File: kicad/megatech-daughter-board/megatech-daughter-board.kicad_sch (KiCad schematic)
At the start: 41 parts, among them CN1 JST NH 7P, CN2 DB25_Socket, CN3 Conn_02x20_Counter_Clockwise, IC1 Z084000xP, IC2 NEC D71051C, IC3 HC393, IC4 HC04, IC5 PAL16L8A, IC6 µPD4711C, X1 4.9152 MHz

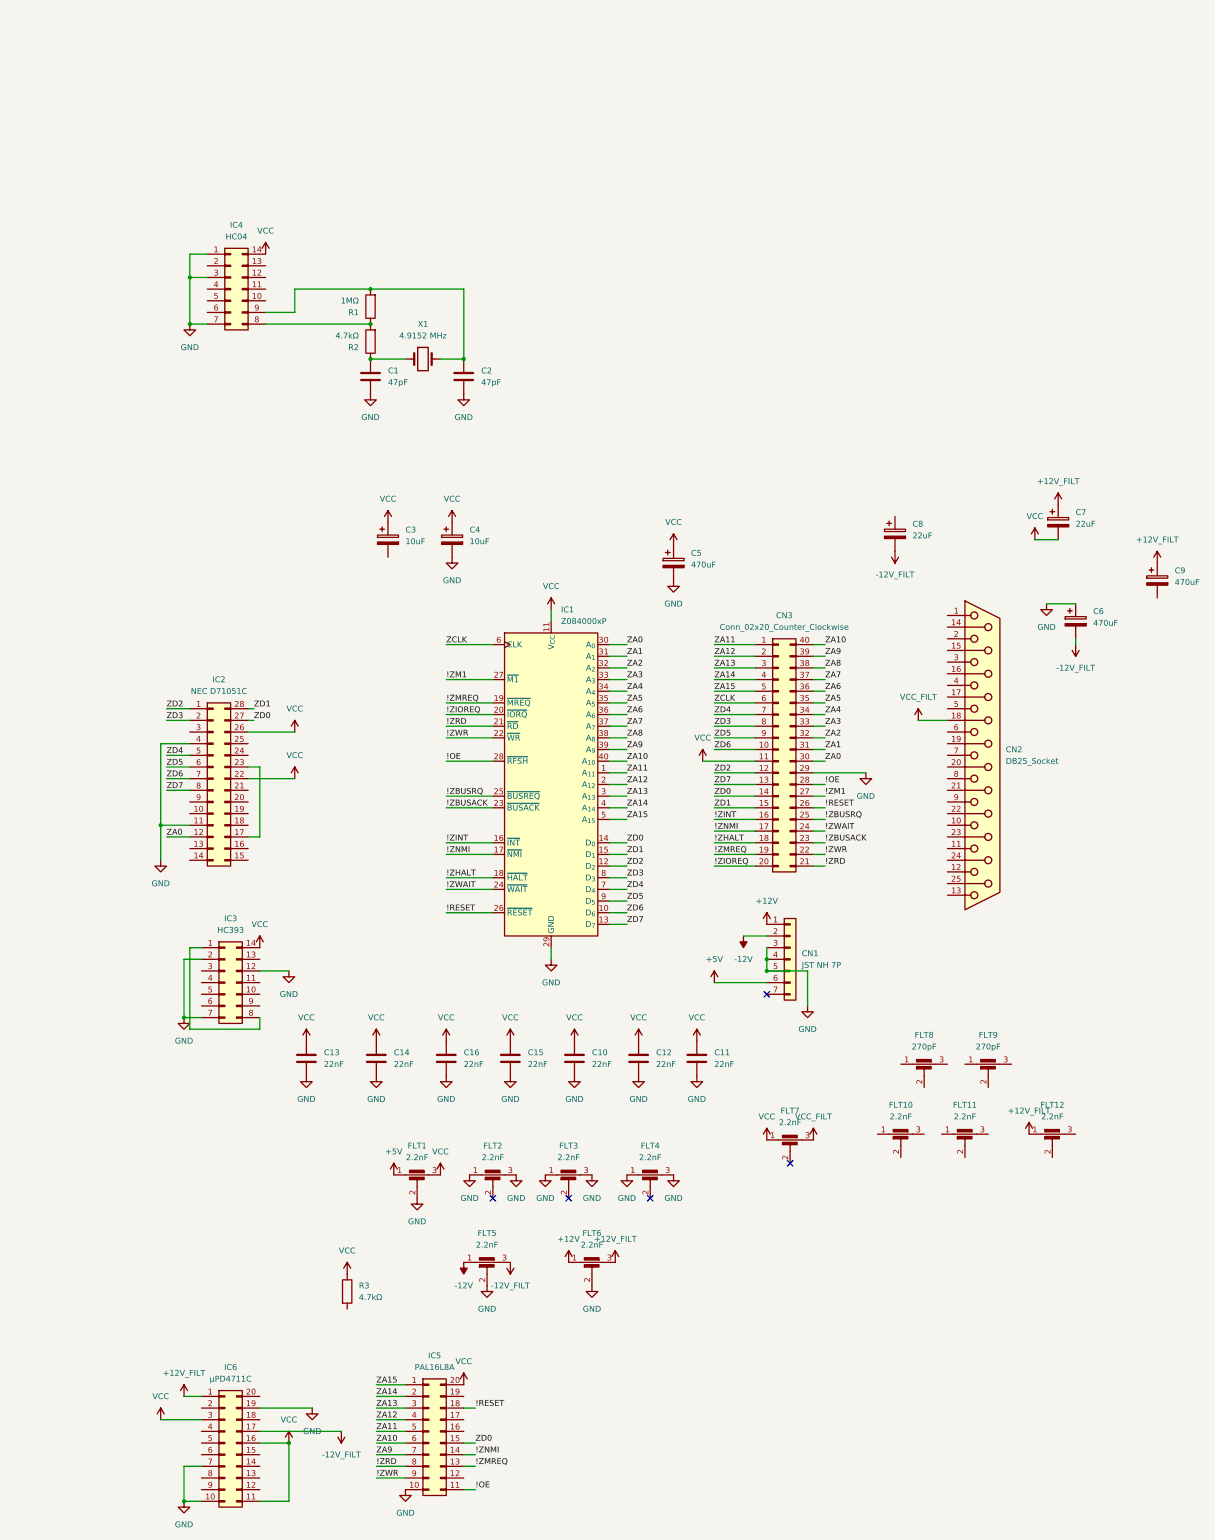
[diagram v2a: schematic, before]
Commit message: Further updates to the daughterboard pcb
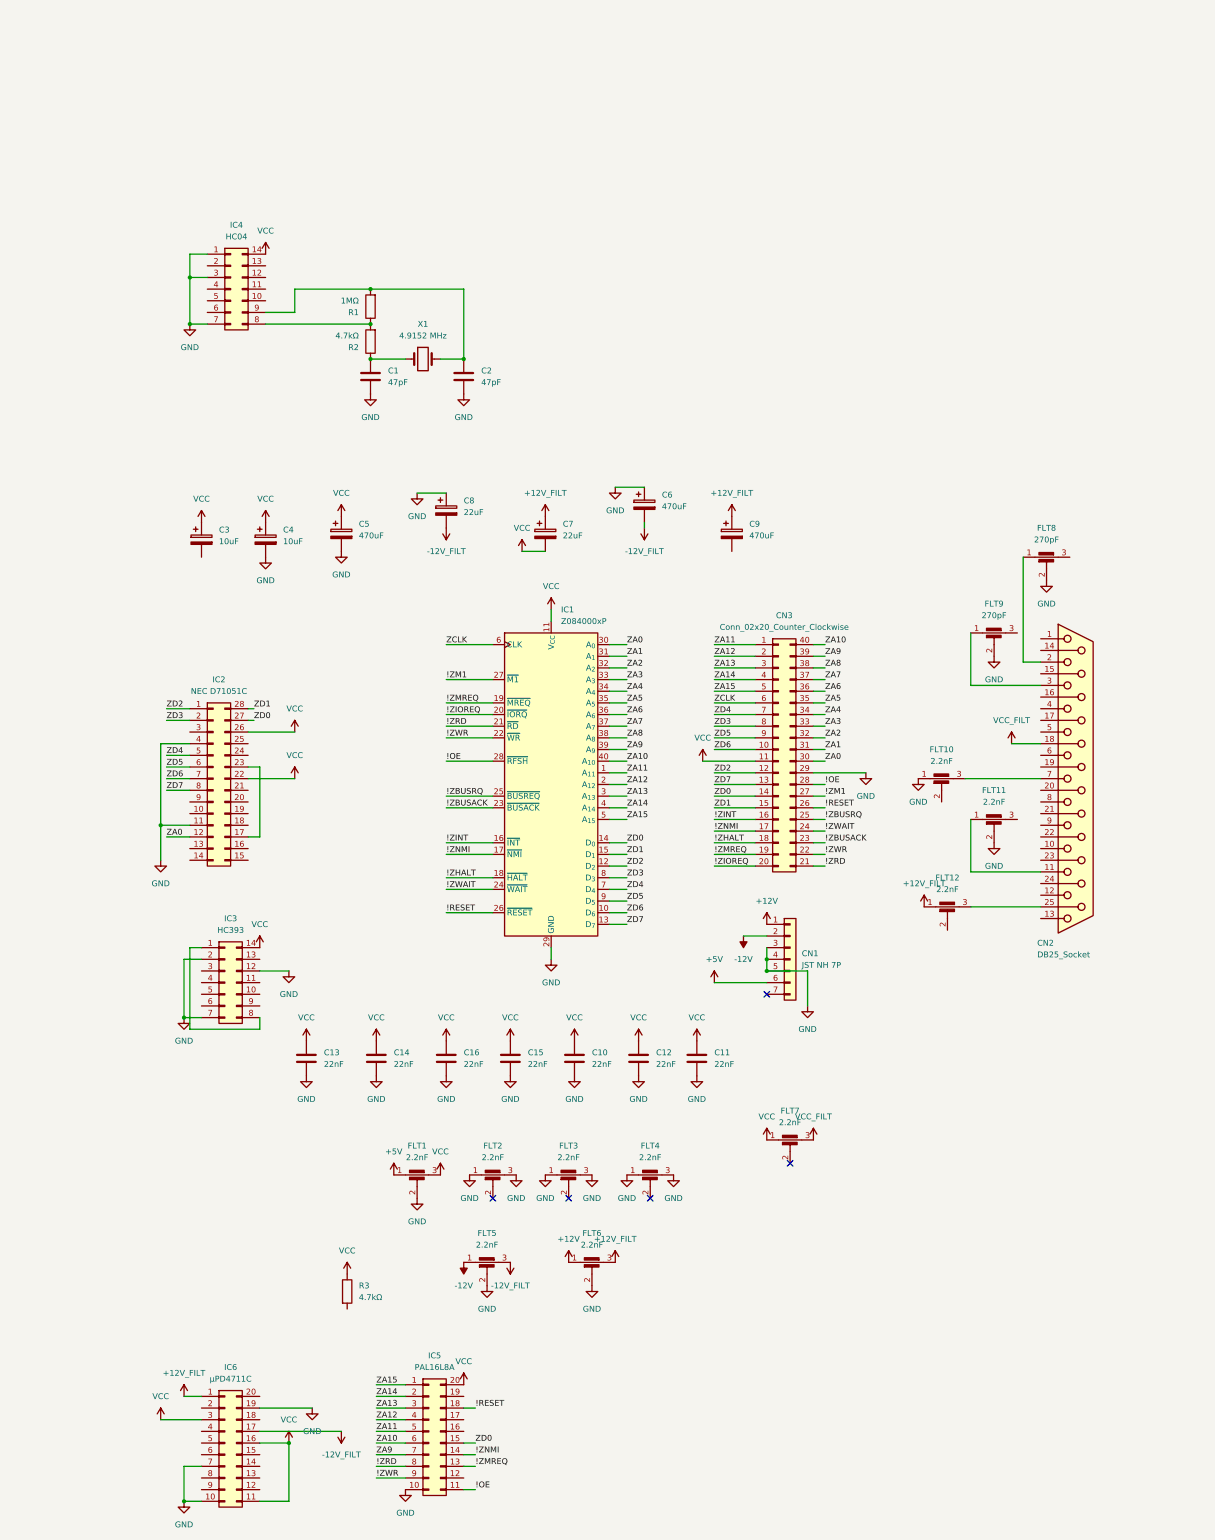
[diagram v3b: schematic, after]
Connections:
- net GND: now also C8.1, FLT10.1, FLT11.2, FLT8.2, FLT9.2
- net at CN2.11: now also FLT11.1
- net at CN2.2: now also FLT8.1
- net at CN2.25 (P25): now also FLT12.3
- net at CN2.3: now also FLT9.1
- net at CN2.7: now also FLT10.3
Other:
- moved on the sheet: C3, C4, C5, C6, C7, C8, C9, CN2, FLT10, FLT11, FLT12, FLT8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

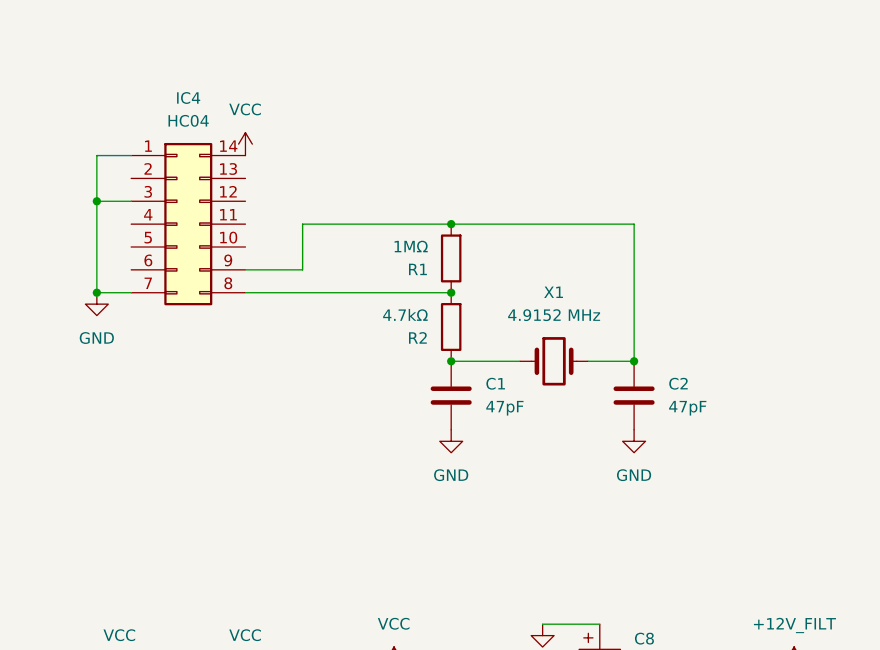
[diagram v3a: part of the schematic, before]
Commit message: Further improvements to daughter board pcb
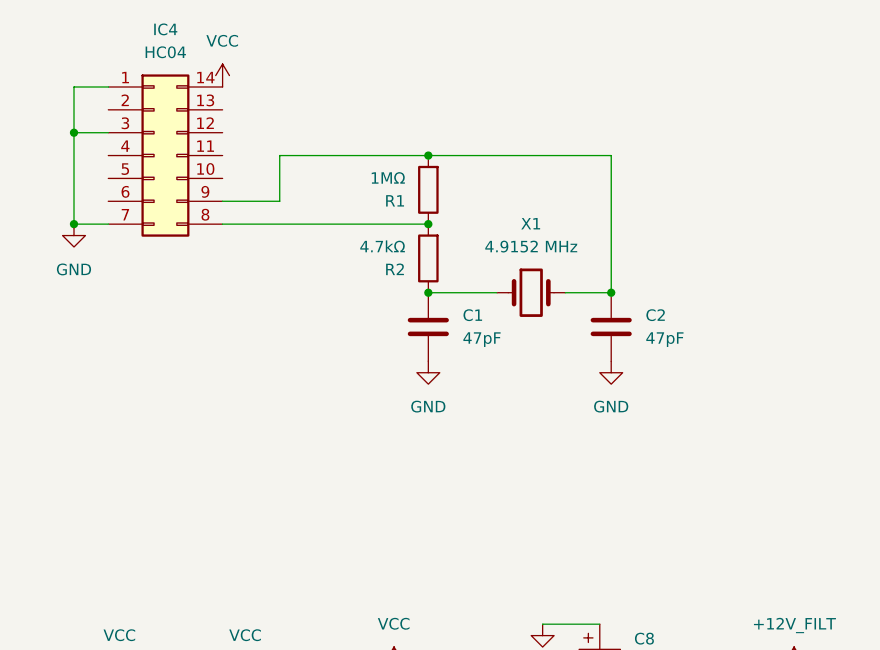
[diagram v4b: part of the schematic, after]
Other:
- moved on the sheet: C1, C2, IC4, R1, R2, X1

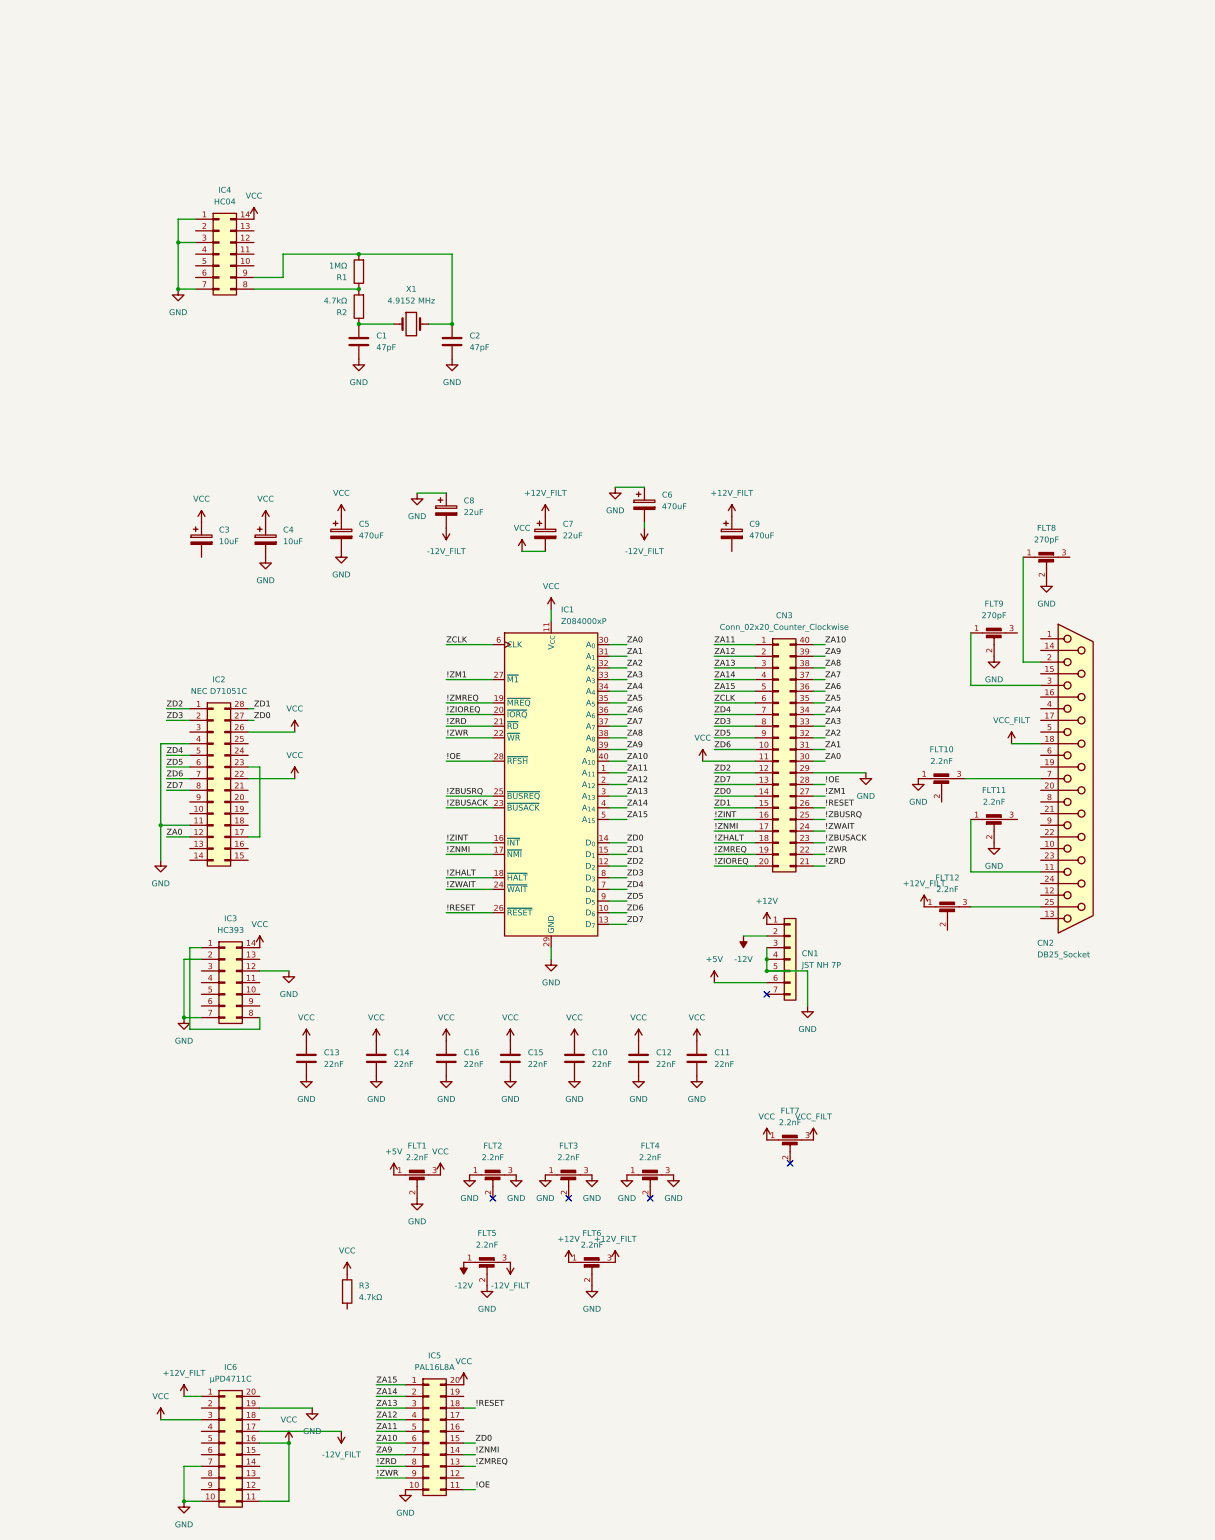
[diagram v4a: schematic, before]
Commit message: Correct FLT7 on daughter board
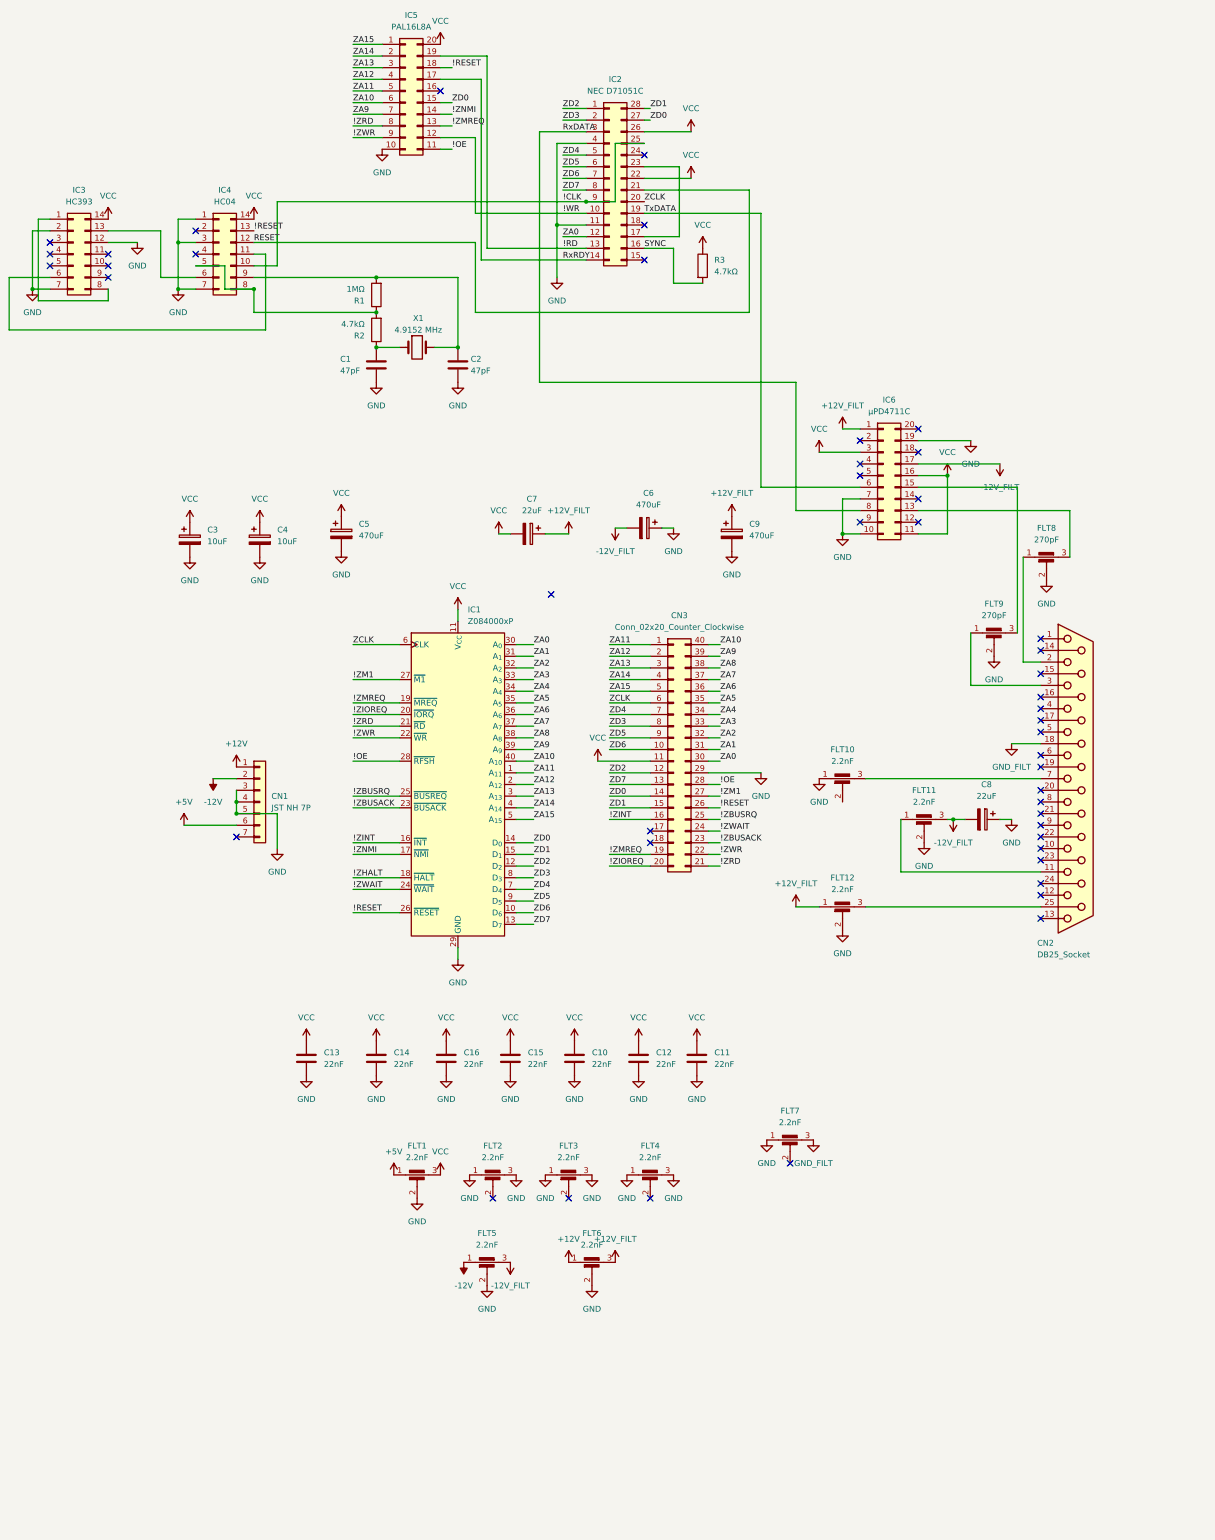
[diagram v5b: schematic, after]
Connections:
- net !RESET: now also IC4.13 (Pin_13)
- net !ZHALT: no longer CN3.18 (Pin_18)
- net !ZNMI: no longer CN3.17 (Pin_17)
- net -12V_FILT: now also FLT11.3
- net GND: now also C3.2, C9.2, FLT12.2, FLT7.1
- net VCC: no longer FLT7.1
- net ZCLK: now also IC2.20 (Pin_20)
- net !WR: now reaches IC5.12 (Pin_12)
- net !WR: now also IC2.10 (Pin_10)
- net RxRDY: now reaches IC5.17 (Pin_17)
- net RxRDY: now also IC2.14 (Pin_14)
- net !RD: now reaches IC5.19 (Pin_19)
- net !RD: now also IC2.13 (Pin_13)
- net at IC4.8 (Pin_8), R1.1, R2.2: now also IC4.5 (Pin_5)
- net at FLT8.3: now also IC6.13 (Pin_13)
- net at IC3.13 (Pin_13): now also IC4.6 (Pin_6)
- net at IC3.6 (Pin_6): now also IC4.11 (Pin_11)
- net SYNC: now reaches R3.2
- net SYNC: now also IC2.16 (Pin_16)
- net at FLT9.3: now also IC6.15 (Pin_15)
- net TxDATA: now reaches IC2.19 (Pin_19)
- net TxDATA: now also IC6.6 (Pin_6)
- net RESET: now reaches IC2.21 (Pin_21)
- net RESET: now also IC4.12 (Pin_12)
- net !CLK: now reaches IC2.25 (Pin_25)
- net !CLK: now also IC2.9 (Pin_9), IC4.10 (Pin_10)
- net RxDATA: now reaches IC2.3 (Pin_3)
- net RxDATA: now also IC6.8 (Pin_8)
- net VCC_FILT renamed GND_FILT
- no-connect marks 5 -> 47
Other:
- moved on the sheet: C1, C2, C3, C4, C6, C7, C8, CN1, CN3, FLT10, FLT11, FLT12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
